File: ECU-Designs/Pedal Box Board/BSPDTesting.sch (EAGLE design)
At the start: 16 parts, among them X1 MINIFIT_5566-2, X2 MINIFIT_5566-2

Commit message: Huge WIP, converting o a 10 minifit
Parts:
- removed BATTERY: MINIFIT_5566-2, HyTechDevices:MINIFIT_5566-2
- removed S1, S2, S3: (no value), HyTechDevices:BTN_10-XX
- added BSPDTESTING: MINIFIT_5566-10, HyTechDevices:MINIFIT_5566-10
- added U$1, U$2, U$3: 0S102011MS2QS1, HyTechDevices:0S102011MS2QS1
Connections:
- removed net N$11: S1.P, X1-2.S
- removed net N$12: S2.P, X2-2.S
- removed net N$7: IC1.IN, S3.S
- net GND: now also BSPDTESTING-10.S, TRIPPED.C; no longer BATTERY-2.S, R3.2, R4.1
- net N$1: now also BSPDTESTING-1.S, U$1.P; no longer R2.S, S1.S
- net N$2: now also BSPDTESTING-2.S, R3.2; no longer R1.S, S2.S
- net N$3: now also R3.1, TRIPPED.A; no longer BATTERY-1.S, S3.P
- net N$4: now also IC1.IN, U$1.O; no longer IC1.OUT, R1.A, R2.A
- net N$5: now also BSPDTESTING-3.S, U$2.P; no longer R2.E, R3.1
- net N$6: now also BSPDTESTING-4.S, U$3.P; no longer R1.E, R4.2
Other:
- moved on the sheet: IC1, R1, R2, R3, R4, TRIPPED

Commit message: Cleaned up the schematic and made a board....are the LEDs fine?
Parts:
- removed R1, R2: (no value), HyTechDevices:3RP/1610N
- removed TESTINGLEDS: MINIFIT_5566-4, HyTechDevices:MINIFIT_5566-4
- removed U$1, U$2, U$3: 0S102011MS2QS1, HyTechDevices:0S102011MS2QS1
- removed X1, X2: MINIFIT_5566-2, HyTechDevices:MINIFIT_5566-2
- added BRAKE, CURRENT: (no value), HyTechDevices:3RP/1610N
- added POWER_SWITCH: 0S102011MS2QS1, HyTechDevices:0S102011MS2QS1
- added R5, R6: (no value), HyTechDevices:RESISTORAXIAL-0.3
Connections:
- removed net N$5: BSPDTESTING-3.S, U$2.P
- removed net N$6: BSPDTESTING-4.S, U$3.P
- new net +12V: BSPDTESTING-9.S
- new net N$12: R4.2, SWITCH.A
- new net N$13: CHARGE.A, R6.2
- new net N$14: BSPDTESTING-7.S, R6.1
- new net N$15: BRAKE.E, CURRENT.E, IC1.OUT
- new net SIGNAL_BRAKE: BSPDTESTING-4.S
- new net SIGNAL_CURRENT: BSPDTESTING-3.S
- net GND: now also BRAKE.A, CURRENT.A
- net N$1: now also POWER_SWITCH.P; no longer U$1.P
- net N$10: now also BSPDTESTING-6.S, R5.1; no longer SWITCH.A, TESTINGLEDS-3.S
- net N$4: now also POWER_SWITCH.O; no longer U$1.O
- net N$8: now also FAULT.A, R5.2; no longer CHARGE.A, TESTINGLEDS-1.S
- net N$9: now also BSPDTESTING-5.S, R4.1; no longer FAULT.A, TESTINGLEDS-2.S
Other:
- moved on the sheet: CHARGE, FAULT, R3, R4, SWITCH, TRIPPED

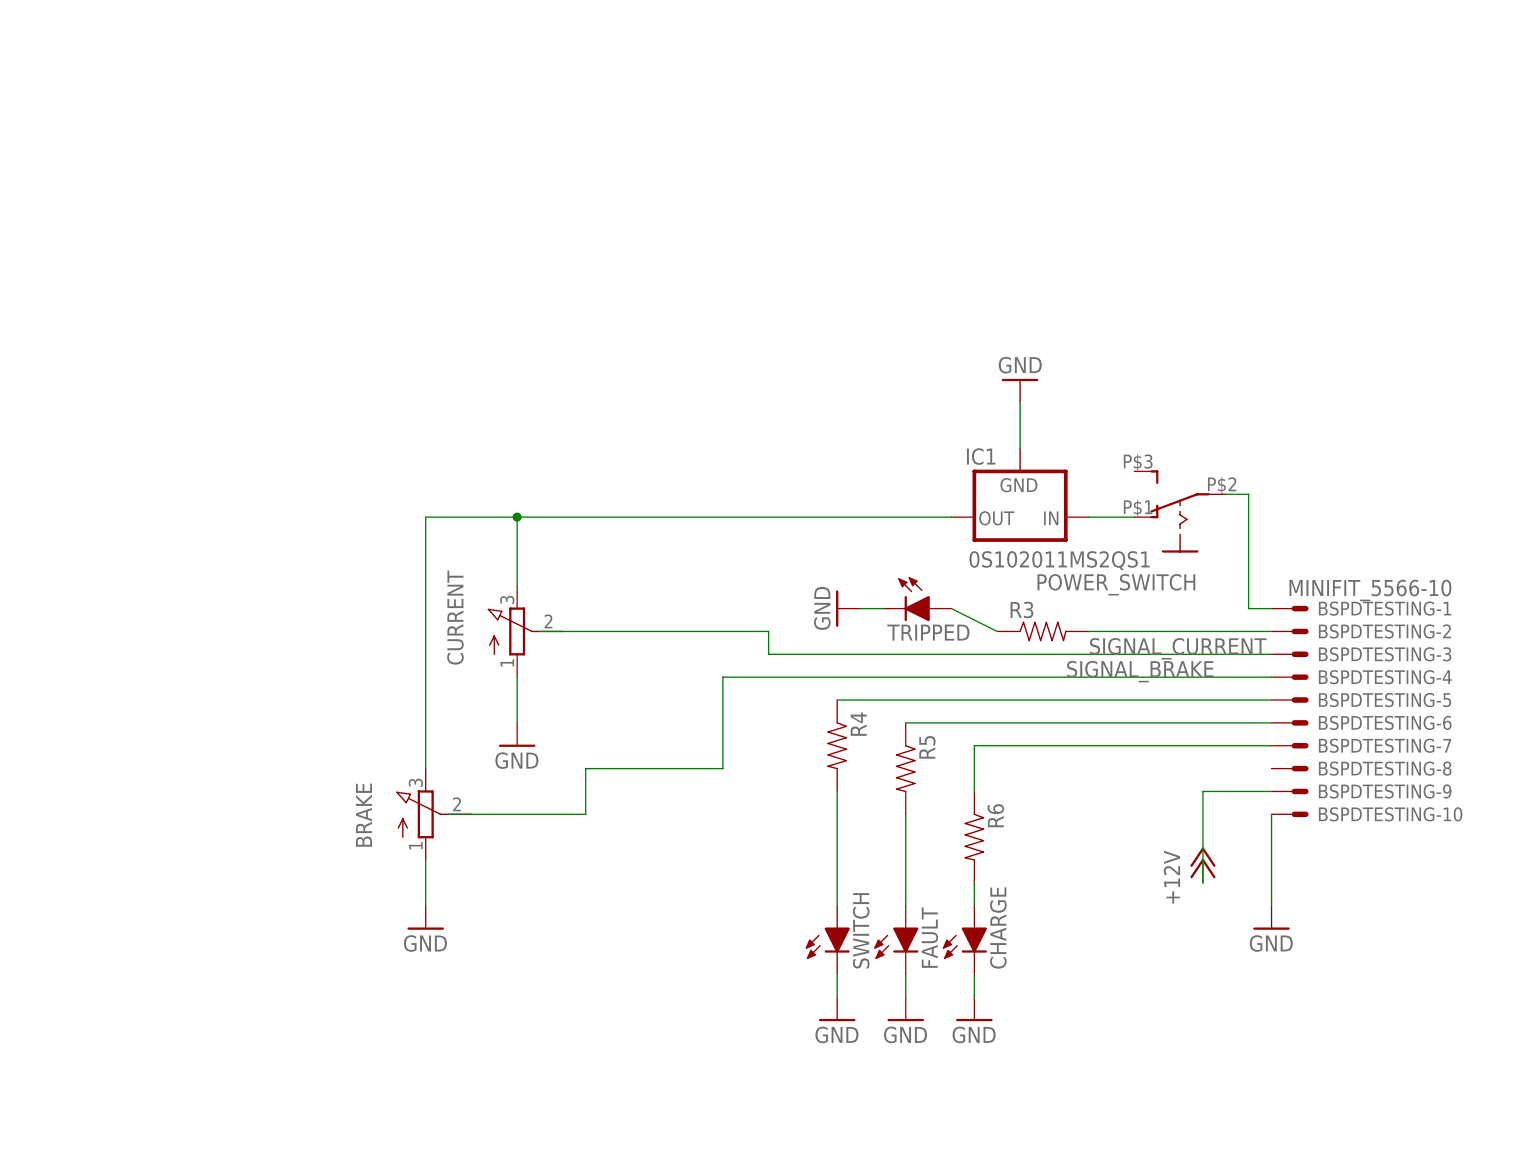
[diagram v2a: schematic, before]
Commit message: Made Revisions, add capacitors on the side of wires where test points would be placed. Found potential testpoints to utilize.
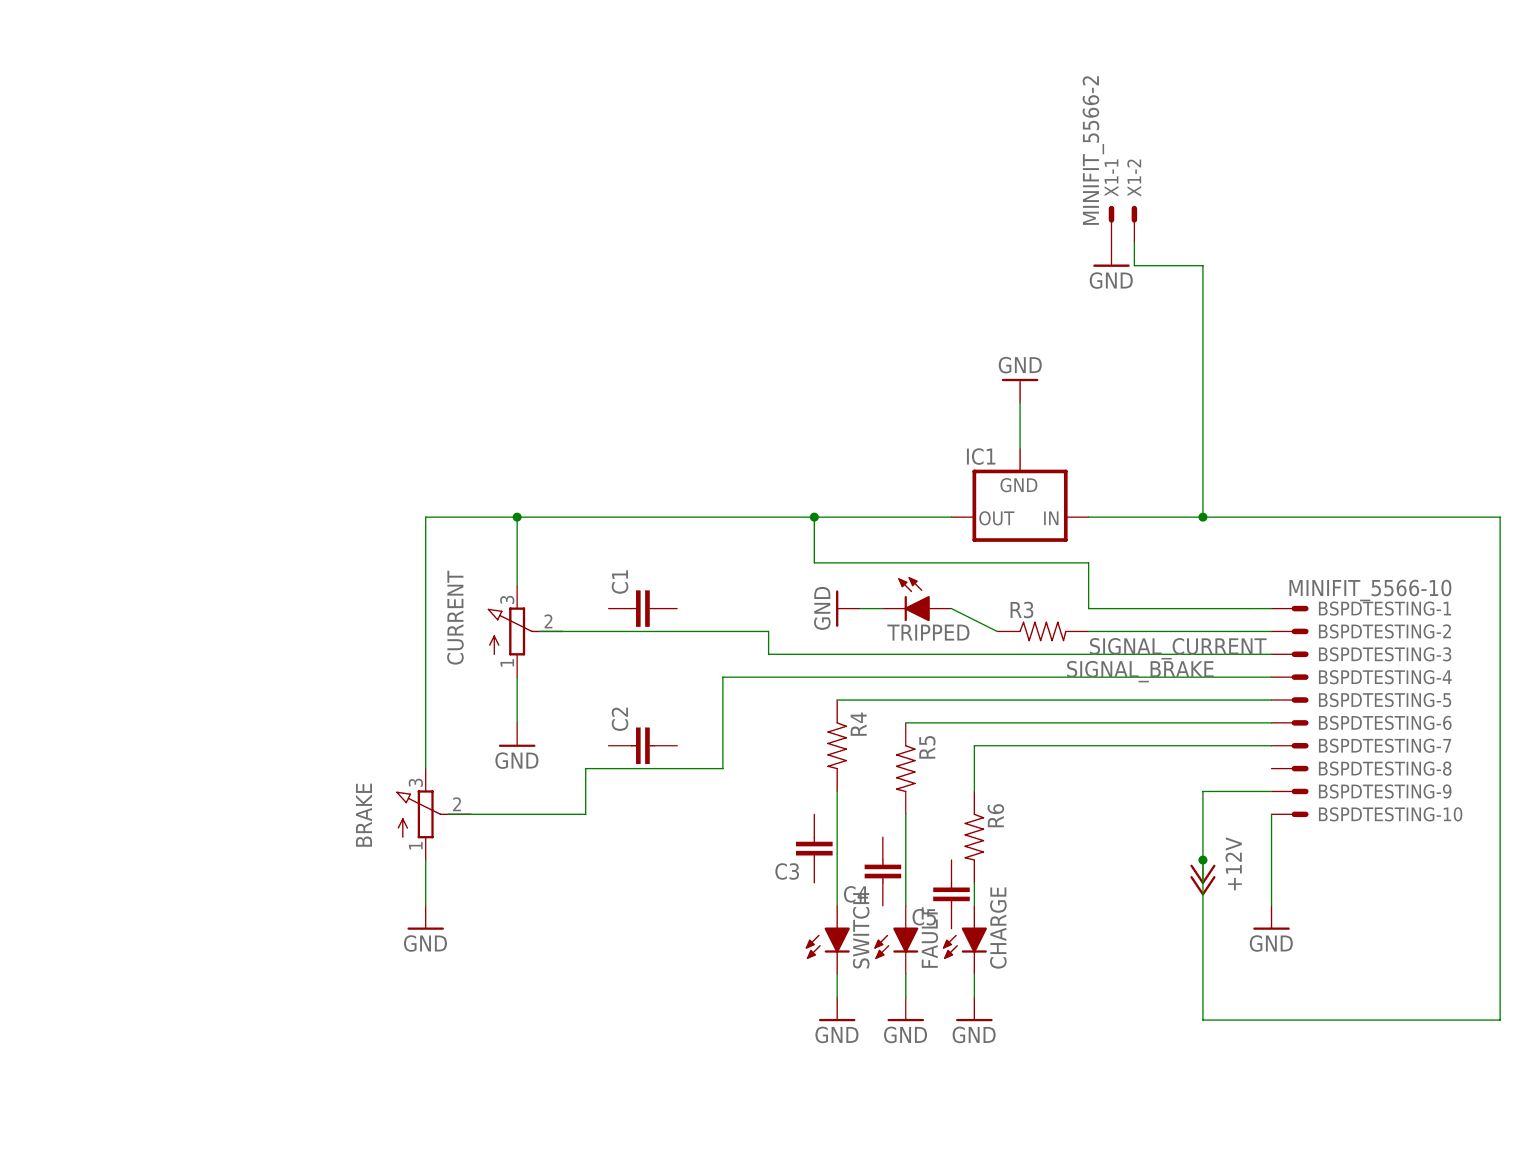
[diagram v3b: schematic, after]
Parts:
- removed POWER_SWITCH: 0S102011MS2QS1, HyTechDevices:0S102011MS2QS1
- added C1, C2, C3, C4, C5: (no value), HyTechDevices:CAPEZ
- added X1: MINIFIT_5566-2, HyTechDevices:MINIFIT_5566-2
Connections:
- removed net N$4: IC1.IN, POWER_SWITCH.O
- net +12V: now also IC1.IN, X1-2.S
- net GND: now also X1-1.S
- net N$1: no longer POWER_SWITCH.P
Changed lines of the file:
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@@
 <part name="GND8" library="supply1" deviceset="GND" device=""/>
 <part name="BSPDTESTING" library="HyTechDevices" deviceset="MINIFIT_5566-10" device=""/>
-<part name="POWER_SWITCH" library="HyTechDevices" deviceset="0S102011MS2QS1" device=""/>
 <part name="R5" library="HyTechDevices" deviceset="RESISTOR" device="AXIAL-0.3"/>
 <part name="R6" library="HyTechDevices" deviceset="RESISTOR" device="AXIAL-0.3"/>
 <part name="P+1" library="supply1" deviceset="+12V" device=""/>
+<part name="X1" library="HyTechDevices" deviceset="MINIFIT_5566-2" device=""/>
+<part name="GND9" library="supply1" deviceset="GND" device=""/>
+<part name="C1" library="HyTechDevices" deviceset="CAP" device="EZ"/>
+<part name="C2" library="HyTechDevices" deviceset="CAP" device="EZ"/>
+<part name="C3" library="HyTechDevices" deviceset="CAP" device="EZ"/>
+<part name="C4" library="HyTechDevices" deviceset="CAP" device="EZ"/>
+<part name="C5" library="HyTechDevices" deviceset="CAP" device="EZ"/>
 </parts>
 <sheets>
@@
 <instance part="BSPDTESTING" gate="-9" x="116.84" y="40.64"/>
 <instance part="BSPDTESTING" gate="-10" x="116.84" y="38.1"/>
-<instance part="POWER_SWITCH" gate="G$1" x="104.14" y="71.12" rot="R90"/>
 <instance part="R5" gate="G$1" x="73.66" y="43.18" rot="R270"/>
 <instance part="R6" gate="G$1" x="81.28" y="35.56" rot="R270"/>
-<instance part="P+1" gate="1" x="106.68" y="33.02"/>
+<instance part="P+1" gate="1" x="106.68" y="30.48" rot="R180"/>
+<instance part="X1" gate="-2" x="99.06" y="104.14" rot="R90"/>
+<instance part="X1" gate="-1" x="96.52" y="104.14" rot="R90"/>
+<instance part="GND9" gate="1" x="96.52" y="99.06"/>
+<instance part="C1" gate="G$1" x="45.72" y="60.96" rot="R90"/>
+<instance part="C2" gate="G$1" x="45.72" y="45.72" rot="R90"/>
+<instance part="C3" gate="G$1" x="63.5" y="35.56" rot="R180"/>
+<instance part="C4" gate="G$1" x="71.12" y="33.02" rot="R180"/>
+<instance part="C5" gate="G$1" x="78.74" y="30.48" rot="R180"/>
 </instances>
 <busses>
@@
 <wire x1="30.48" y1="48.26" x2="30.48" y2="53.34" width="0.1524" layer="91"/>
 </segment>
+<segment>
+<pinref part="X1" gate="-1" pin="S"/>
+<pinref part="GND9" gate="1" pin="GND"/>
+</segment>
 </net>
 <net name="N$1" class="0">
@@
 <pinref part="BSPDTESTING" gate="-1" pin="S"/>
 <wire x1="114.3" y1="60.96" x2="111.76" y2="60.96" width="0.1524" layer="91"/>
-<wire x1="111.76" y1="60.96" x2="111.76" y2="73.66" width="0.1524" layer="91"/>
-<pinref part="POWER_SWITCH" gate="G$1" pin="P"/>
-<wire x1="111.76" y1="73.66" x2="109.22" y2="73.66" width="0.1524" layer="91"/>
 </segment>
 </net>
@@
 <pinref part="TRIPPED" gate="LED" pin="A"/>
 <wire x1="83.82" y1="58.42" x2="78.74" y2="60.96" width="0.1524" layer="91"/>
-</segment>
-</net>
-<net name="N$4" class="0">
-<segment>
-<pinref part="POWER_SWITCH" gate="G$1" pin="O"/>
-<pinref part="IC1" gate="G$1" pin="IN"/>
-<wire x1="99.06" y1="71.12" x2="93.98" y2="71.12" width="0.1524" layer="91"/>
 </segment>
 </net>
@@
 <pinref part="BRAKE" gate="G$1" pin="E"/>
 <pinref part="IC1" gate="G$1" pin="OUT"/>
-<wire x1="78.74" y1="71.12" x2="30.48" y2="71.12" width="0.1524" layer="91"/>
+<wire x1="78.74" y1="71.12" x2="63.5" y2="71.12" width="0.1524" layer="91"/>
 <junction x="30.48" y="71.12"/>
+<wire x1="63.5" y1="71.12" x2="30.48" y2="71.12" width="0.1524" layer="91"/>
+<wire x1="63.5" y1="71.12" x2="63.5" y2="66.04" width="0.1524" layer="91"/>
+<junction x="63.5" y="71.12"/>
+<wire x1="63.5" y1="66.04" x2="93.98" y2="66.04" width="0.1524" layer="91"/>
+<wire x1="93.98" y1="66.04" x2="93.98" y2="60.96" width="0.1524" layer="91"/>
+<wire x1="93.98" y1="60.96" x2="111.76" y2="60.96" width="0.1524" layer="91"/>
 </segment>
 </net>
@@
 <segment>
 <pinref part="P+1" gate="1" pin="+12V"/>
-<wire x1="106.68" y1="30.48" x2="106.68" y2="40.64" width="0.1524" layer="91"/>
+<wire x1="106.68" y1="33.02" x2="106.68" y2="40.64" width="0.1524" layer="91"/>
 <pinref part="BSPDTESTING" gate="-9" pin="S"/>
 <wire x1="106.68" y1="40.64" x2="114.3" y2="40.64" width="0.1524" layer="91"/>
-</segment>
-</net>
+<pinref part="IC1" gate="G$1" pin="IN"/>
+<wire x1="93.98" y1="71.12" x2="106.68" y2="71.12" width="0.1524" layer="91"/>
+<wire x1="106.68" y1="71.12" x2="139.7" y2="71.12" width="0.1524" layer="91"/>
+<wire x1="139.7" y1="71.12" x2="139.7" y2="15.24" width="0.1524" layer="91"/>
+<wire x1="139.7" y1="15.24" x2="106.68" y2="15.24" width="0.1524" layer="91"/>
+<wire x1="106.68" y1="15.24" x2="106.68" y2="33.02" width="0.1524" layer="91"/>
+<junction x="106.68" y="33.02"/>
+<pinref part="X1" gate="-2" pin="S"/>
+<wire x1="99.06" y1="101.6" x2="99.06" y2="99.06" width="0.1524" layer="91"/>
+<wire x1="99.06" y1="99.06" x2="106.68" y2="99.06" width="0.1524" layer="91"/>
+<wire x1="106.68" y1="99.06" x2="106.68" y2="71.12" width="0.1524" layer="91"/>
+<junction x="106.68" y="71.12"/>
+</segment>
+</net>
